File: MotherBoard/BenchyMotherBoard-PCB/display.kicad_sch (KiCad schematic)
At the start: 3 parts, among them J2 LVDS-DISPLAY, U4 AM6254ATCGGAALW, U5 SiI9022ACNU

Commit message: (WIP) More work on power supply sequencing
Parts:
- added J6: HDMI_A_1.4, Daxxn_Connectors:10029449111_AMP, symbol Connector:HDMI_A_1.4
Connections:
- net GND: now also J2.31 (LED-), J2.32 (LED-), J6.11 (CKS), J6.17 (GND), J6.2 (D2S), J6.5 (D1S), J6.8 (D0S), J6.SH
- net DSS-D15: now reaches U5.14 (D15)
- net DSS-D15: now also U4.AA21 (VOUT0-DATA15)
- net DSS-D14: now reaches U5.15 (D14)
- net DSS-D14: now also U4.Y22 (VOUT0-DATA14)
- net DSS-D13: now reaches U5.16 (D13)
- net DSS-D13: now also U4.AA24 (VOUT0-DATA13)
- net DSS-D12: now reaches U5.17 (D12)
- net DSS-D12: now also U4.AB25 (VOUT0-DATA12)
- net DSS-D11: now reaches U5.18 (D11)
- net DSS-D11: now also U4.AA23 (VOUT0-DATA11)
- net DSS-D10: now reaches U5.19 (D10)
- net DSS-D10: now also U4.V20 (VOUT0-DATA10)
- net DSS-D9: now reaches U5.20 (D9)
- net DSS-D9: now also U4.W21 (VOUT0-DATA9)
- net DSS-PCLK: now reaches U5.22 (IDCK)
- net DSS-PCLK: now also U4.AC24 (VOUT0-PCLK)
- net DSS-D8: now reaches U5.23 (D8)
- net DSS-D8: now also U4.V21 (VOUT0-DATA8)
- net DSS-D7: now reaches U5.24 (D7)
- net DSS-D7: now also U4.AA25 (VOUT0-DATA7)
- net DSS-D6: now reaches U5.25 (D6)
- net DSS-D6: now also U4.Y23 (VOUT0-DATA6)
- net DSS-D5: now reaches U5.27 (D5)
- net DSS-D5: now also U4.Y24 (VOUT0-DATA5)
- net DSS-D4: now reaches U5.28 (D4)
- net DSS-D4: now also U4.Y25 (VOUT0-DATA4)
- net DSS-D3: now reaches U5.29 (D3)
- net DSS-D3: now also U4.W24 (VOUT0-DATA3)
- net DSS-D2: now reaches U5.30 (D2)
- net DSS-D2: now also U4.W25 (VOUT0-DATA2)
- net DSS-D1: now reaches U5.31 (D1)
- net DSS-D1: now also U4.V24 (VOUT0-DATA1)
- net DSS-D0: now reaches U5.32 (D0)
- net DSS-D0: now also U4.U22 (VOUT0-DATA0)
- net DSS-DE: now reaches U5.33 (DE)
- net DSS-DE: now also U4.Y20 (VOUT0-DE)
- net DSS-HSYNC: now reaches U5.34 (HSYNC)
- net DSS-HSYNC: now also U4.AB24 (VOUT0-HSYNC)
- net DSS-VSYNC: now reaches U5.35 (VSYNC)
- net DSS-VSYNC: now also U4.AC25 (VOUT0-VSYNC)
- net HDMI-SDA: now reaches U5.48 (DSDA)
- net HDMI-SCL: now reaches U5.49 (DSCL)
- net HDMI-HPD: now reaches U5.54 (HPD)
- net HDMI-HPD: now also J6.19 (HPD/HEAC-)
- net HDMI-TXC-: now reaches U5.58 (TXC-)
- net HDMI-TXC-: now also J6.12 (CK-)
- net HDMI-TXC+: now reaches U5.59 (TXC+)
- net HDMI-TXC+: now also J6.10 (CK+)
- net HDMI-TX0-: now reaches U5.61 (TX0-)
- net HDMI-TX0-: now also J6.9 (D0-)
- net HDMI-TX0+: now reaches U5.62 (TX0+)
- net HDMI-TX0+: now also J6.7 (D0+)
- net HDMI-TX1-: now reaches U5.64 (TX1-)
- net HDMI-TX1-: now also J6.6 (D1-)
- net HDMI-TX1+: now reaches U5.65 (TX1+)
- net HDMI-TX1+: now also J6.4 (D1+)
- net HDMI-TX2-: now reaches U5.67 (TX2-)
- net HDMI-TX2-: now also J6.3 (D2-)
- net HDMI-TX2+: now reaches U5.68 (TX2+)
- net HDMI-TX2+: now also J6.1 (D2+)
- net HDMI-CECA: now reaches U5.71 (CEC-A)
- net LVDS-D0-: now reaches U4.AA5 (OLDI0-A0N)
- net LVDS-D0-: now also J2.8 (LVDS-D0-)
- net LVDS-D3+: now reaches U4.AA7 (OLDI0-A3P)
- net LVDS-D3+: now also J2.21 (LVDS-D3+)
- net LVDS-D2+: now reaches U4.AA8 (OLDI0-A2P)
- net LVDS-D2+: now also J2.15 (LVDS-D2+)
- net LVDS-D1+: now reaches U4.AB4 (OLDI0-A1P)
- net LVDS-D1+: now also J2.12 (LVDS-D1+)
- net LVDS-D3-: now reaches U4.AB6 (OLDI0-A3N)
- net LVDS-D3-: now also J2.20 (LVDS-D3-)
- net LVDS-D1-: now reaches U4.AD3 (OLDI0-A1N)
- net LVDS-D1-: now also J2.11 (LVDS-D1-)
- net LVDS-CLK-: now reaches U4.AD4 (OLDI0-CLK0N)
- net LVDS-CLK-: now also J2.17 (LVDS-CLK-)
- net LVDS-CLK+: now reaches U4.AE3 (OLDI0-CLK0P)
- net LVDS-CLK+: now also J2.18 (LVDS-CLK+)
- net LVDS-D0+: now reaches U4.Y6 (OLDI0-A0P)
- net LVDS-D0+: now also J2.9 (LVDS-D0+)
- net LVDS-D2-: now reaches U4.Y8 (OLDI0-A2N)
- net LVDS-D2-: now also J2.14 (LVDS-D2-)
- net at J2.39 (LED+): now also J2.40 (LED+)
- net ~{HDMI-RESET}: now reaches U5.51 (~{RESET})
- net ~{HDMI-INT}: now reaches U5.52 (INT)
- new net VCC: J6.18 (+5V)
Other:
- moved on the sheet: U4H, U5B, U5C

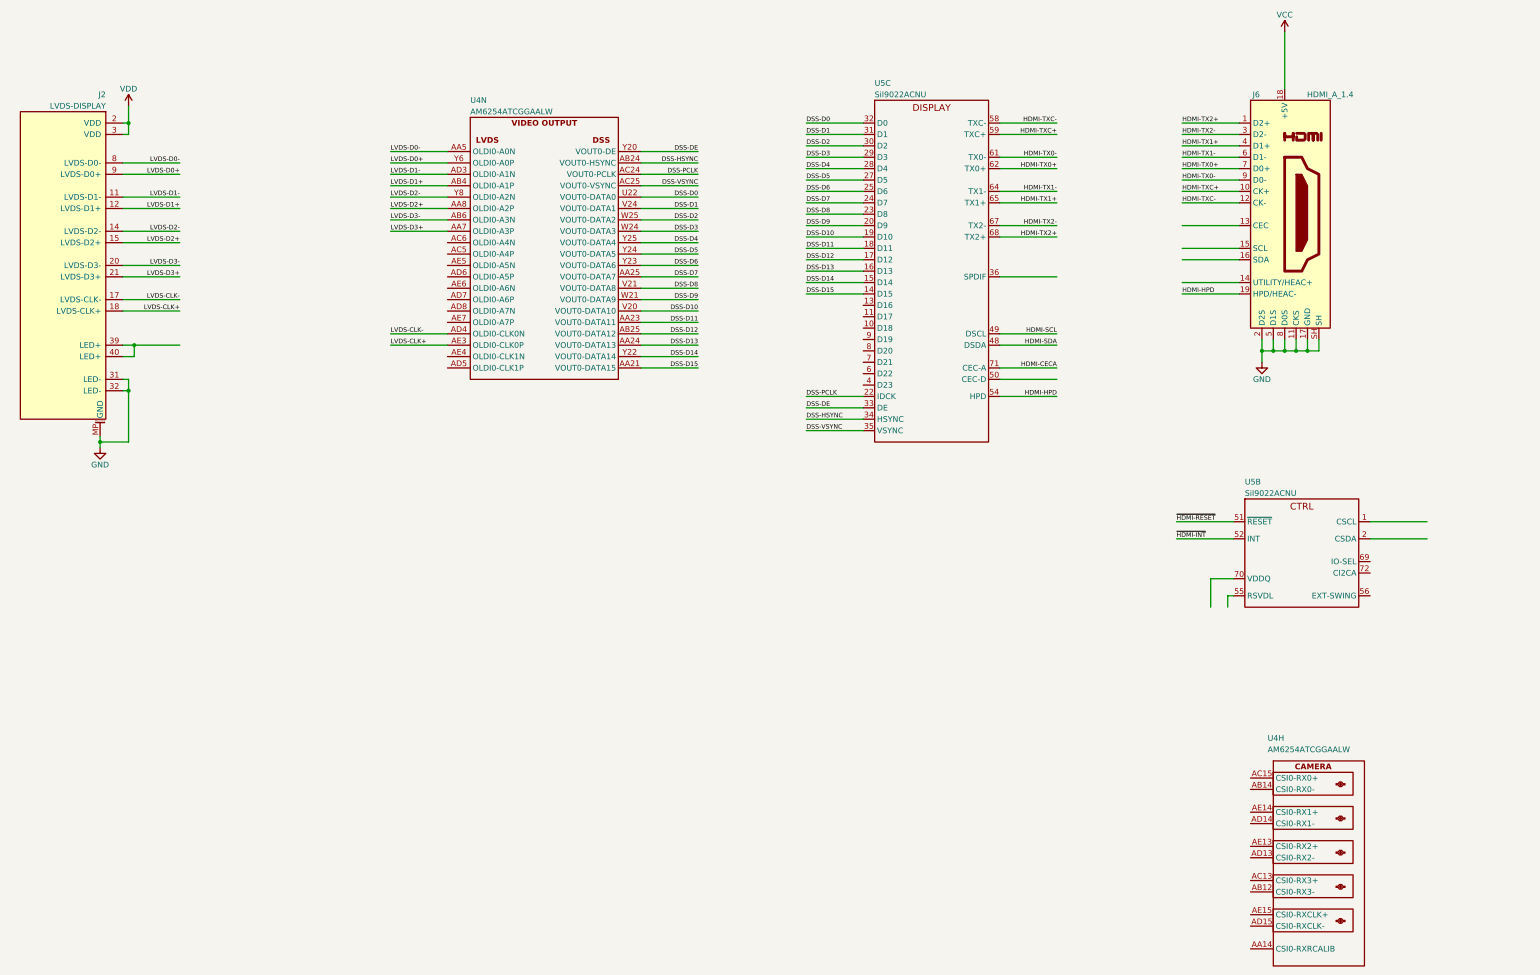
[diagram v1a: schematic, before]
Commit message: (WIP) Complete most of the PS and boot schematics
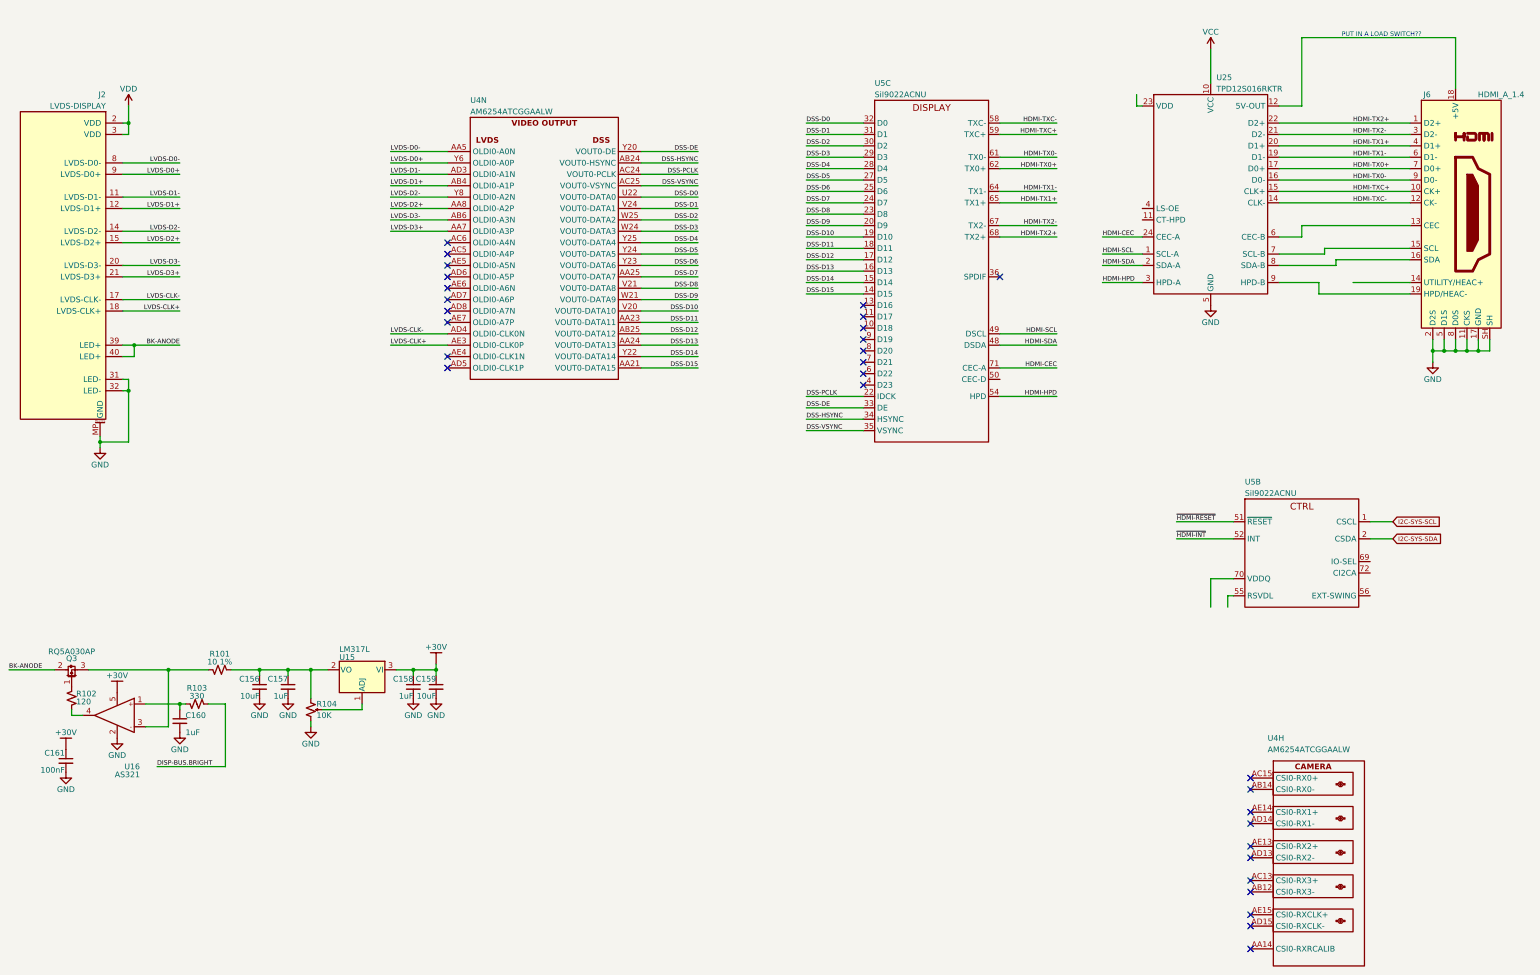
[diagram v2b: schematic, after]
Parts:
- added C156, C159: 10uF, Capacitor_SMD:C_1210_3225Metric, symbol Daxxn_Device:C
- added C157, C158, C160: 1uF, Capacitor_SMD:C_0805_2012Metric, symbol Daxxn_Device:C
- added C161: 100nF, Capacitor_SMD:C_0805_2012Metric, symbol Daxxn_Device:C
- added Q3: RQ5A030AP, Package_TO_SOT_SMD:SOT-23, symbol Daxxn_Transistors:RQ5A030AP
- added R101: 10 1%, Resistor_SMD:R_0805_2012Metric, symbol Daxxn_Device:R
- added R102: 120, Resistor_SMD:R_0805_2012Metric, symbol Daxxn_Device:R
- added R103: 330, Resistor_SMD:R_0805_2012Metric, symbol Daxxn_Device:R
- added R104: 10K, Daxxn_Switches:Bourns_TC33X, symbol Daxxn_Device:R_Pot
- added U15: LM317L, Package_TO_SOT_SMD:SOT-89-3, symbol Regulator_Linear:LM317L_SOT-89
- added U16: AS321, Package_TO_SOT_SMD:SOT-23-5, symbol Daxxn_OPAMP:AS321
- added U25: TPD12S016RKTR, Daxxn_Packages:UQFN-24_4x2mm_P0.5mm, symbol Daxxn_Protection:TPD12S016RKTR
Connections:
- net GND: now also C156.2, C157.2, C158.2, C159.2, C160.2, C161.2, R104.3, U16.2 (V-), U25.13 (GND), U25.18 (GND), U25.5 (GND)
- net HDMI-HPD: now also U25.3 (HPD-A); no longer J6.19 (HPD/HEAC-)
- net HDMI-SCL: now also U25.1 (SCL-A)
- net HDMI-SDA: now also U25.2 (SDA-A)
- net HDMI-TX0+: now also U25.17 (D0+)
- net HDMI-TX0-: now also U25.16 (D0-)
- net HDMI-TX1+: now also U25.20 (D1+)
- net HDMI-TX1-: now also U25.19 (D1-)
- net HDMI-TX2+: now also U25.22 (D2+)
- net HDMI-TX2-: now also U25.21 (D2-)
- net HDMI-TXC+: now also U25.15 (CLK+)
- net HDMI-TXC-: now also U25.14 (CLK-)
- net VCC: now also U25.10 (VCC); no longer J6.18 (+5V)
- net at J6.13 (CEC): now also U25.6 (CEC-B)
- net at J6.15 (SCL): now also U25.7 (SCL-B)
- net at J6.16 (SDA): now also U25.8 (SDA-B)
- net BK-ANODE: now reaches J2.39 (LED+), J2.40 (LED+)
- net BK-ANODE: now also Q3.2 (S)
- net I2C-SYS-SCL: now reaches U5.1 (CSCL)
- net I2C-SYS-SDA: now reaches U5.2 (CSDA)
- net HDMI-CECA renamed HDMI-CEC
- net HDMI-CEC: now also U25.24 (CEC-A)
- new net: R102.1, U16.4 (OUT)
- new net: Q3.1 (G), R102.2
- new net: C160.1, R103.2, U16.1 (IN+)
- new net: R104.2, U15.1 (ADJ)
- new net: C156.1, C157.1, R101.1, R104.1, U15.2 (VO)
- new net: Q3.3 (D), R101.2, U16.3 (IN-)
- new net: J6.18 (+5V), U25.12 (5V-OUT)
- new net: J6.19 (HPD/HEAC-), U25.9 (HPD-B)
- new net +30V: C158.1, C159.1, C161.1, U15.3 (VI), U16.5 (V+)
- new net DISP-BUS.BRIGHT: R103.1
- no-connect marks 0 -> 30
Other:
- note added: "PUT IN A LOAD SWITCH??"
- moved on the sheet: J6

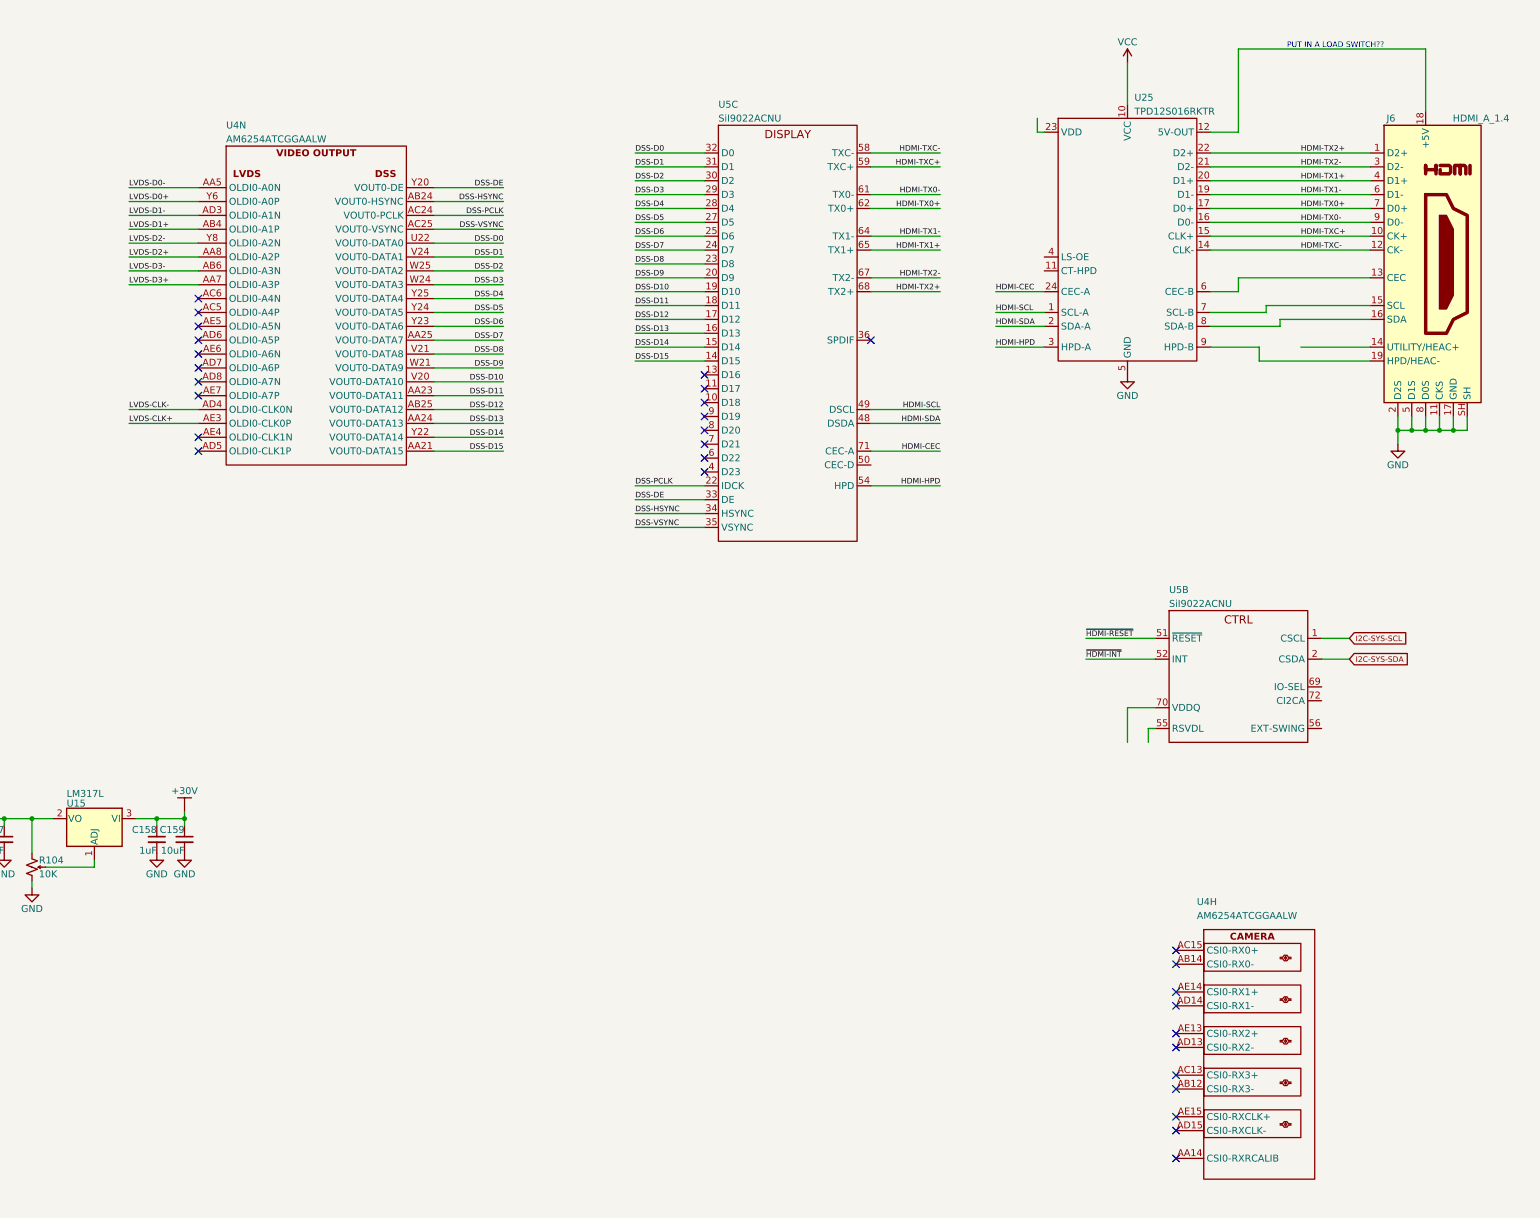
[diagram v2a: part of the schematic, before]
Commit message: Add new ethernet chip - KSZ9031
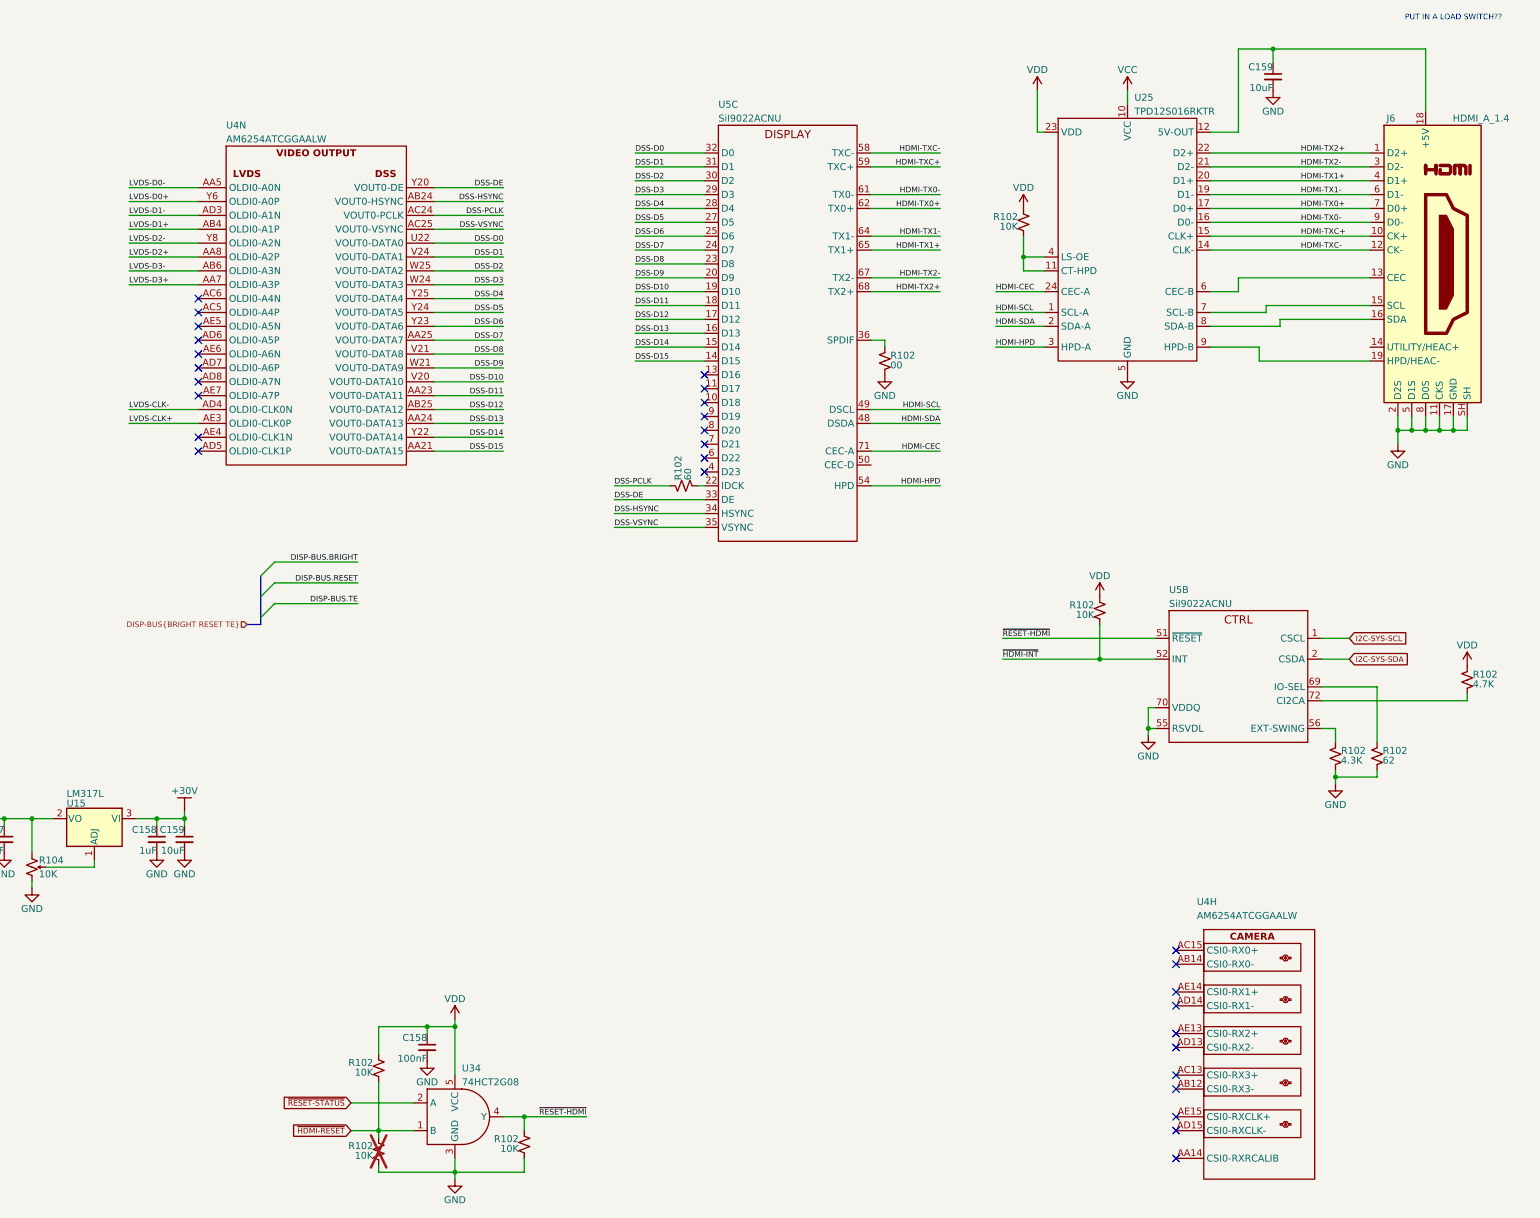
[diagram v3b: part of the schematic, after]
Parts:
- added C158: 100nF, Capacitor_SMD:C_0201_0603Metric, symbol Daxxn_Device:C
- added C159: 10uF, Capacitor_SMD:C_1210_3225Metric, symbol Daxxn_Device:C
- added R102 (x5): 10K, Resistor_SMD:R_0402_1005Metric, symbol Daxxn_Device:R
- added R102: 62, Resistor_SMD:R_0402_1005Metric, symbol Daxxn_Device:R
- added R102: 4.3K, Resistor_SMD:R_0402_1005Metric, symbol Daxxn_Device:R
- added R102: 00, Resistor_SMD:R_0402_1005Metric, symbol Daxxn_Device:R
- added R102: 60, Resistor_SMD:R_0402_1005Metric, symbol Daxxn_Device:R
- added R102: 4.7K, Resistor_SMD:R_0402_1005Metric, symbol Daxxn_Device:R
- added U34: 74HCT2G08, Daxxn_Packages:SOT-353_SC-70-5, symbol Daxxn_Logic:74LVC1G08GW
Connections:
- net DSS-PCLK: now also R102.2; no longer U5.22 (IDCK)
- net GND: now also U5.55 (RSVDL), U5.70 (VDDQ), C158.2, C159.2, R102.1, R102.1, R102.1, R102.1, R102.1, U34.3 (GND)
- net VDD: now also U25.23 (VDD), C158.1, R102.2, R102.2, R102.2, R102.2, U34.5 (VCC)
- net ~{HDMI-INT}: now also R102.1
- net ~{HDMI-RESET}: now also R102.1, R102.2, U34.1 (B); no longer U5.51 (~{RESET})
- net at U5.36 (SPDIF): now also R102.2
- net at U25.11 (CT-HPD): now also U25.4 (LS-OE), R102.1
- net at J6.18 (+5V), U25.12 (5V-OUT): now also C159.1
- net at U5.56 (EXT-SWING): now also R102.2
- net at U5.69 (IO-SEL): now also R102.2
- net at U5.72 (CI2CA): now also R102.1
- new net: R102.1, U5.22 (IDCK)
- new net ~{RESET-HDMI}: R102.2, U34.4 (Y), U5.51 (~{RESET})
- new net ~{RESET-STATUS}: U34.2 (A)
- no-connect marks 30 -> 29

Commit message: (WIP) Almost done with schematic
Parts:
- added C158 (x2): 1uF, Capacitor_SMD:C_0805_2012Metric, symbol Daxxn_Device:C
- added C158 (x4): 100nF, Capacitor_SMD:C_0201_0603Metric, symbol Daxxn_Device:C
- added C158: 10nF, Capacitor_SMD:C_0603_1608Metric, symbol Daxxn_Device:C
- added FB10: 100 @ 100MHz, Inductor_SMD:L_0603_1608Metric, symbol Daxxn_Device:FerriteBead
- J2: footprint (none) -> Daxxn_Connectors:0541324033
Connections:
- net GND: now also C158.1, C158.2, C158.2, C158.2, C158.2, C158.2, C158.2, FB10.1; no longer J6.SH
- net VCC: now also C158.1, C158.1
- net VDD: now also C158.1, C158.1, C158.1, C158.1
- net DISP-BUS.BRIGHT renamed LVDS-BRIGHT
- new net HDMI-SHIELD: C158.2, FB10.2, J6.SH
- no-connect marks 29 -> 31
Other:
- note added: "CHECK OVER!!"
- moved on the sheet: C156, C157, C158, C159, C160, C161, Q3, R101, R102, R103, R104, U15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
